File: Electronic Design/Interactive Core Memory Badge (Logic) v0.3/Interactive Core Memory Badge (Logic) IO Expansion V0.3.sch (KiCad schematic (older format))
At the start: 22 parts, among them J5 Conn_01x04_Female, J7 Conn_01x04_Male, U5 MCP23017_SO, U6 MCP23017_SO, U8 74HC14, U9 74HC14, X1 SAO_v169bis, X2 SAO_v169bis, X3 SAO_v169bis

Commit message: Add I2C Hall sensor, data sheets, sample code
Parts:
- U8, U9: value 74HC14 -> 74AC04
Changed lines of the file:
@@
 AR Path="/5EA63449/5EAA2FDC" Ref="U8"  Part="1"
 F 0 "U8" H 6000 1420 50  0000 C CNN
-F 1 "74HC14" H 6000 1327 50  0000 C CNN
+F 1 "74AC04" H 6000 1327 50  0000 C CNN
 F 2 "Digikey:SOIC-14_W3.9mm" H 6000 1100 50  0001 C CNN
-F 3 "http://www.ti.com/lit/gpn/sn74HC14" H 6000 1100 50  0001 C CNN
+F 3 "http://www.ti.com/lit/gpn/sn74AC04" H 6000 1100 50  0001 C CNN
 	1    6000 1100
 	1    0    0    -1
@@
 AR Path="/5EA63449/5EAA2FE4" Ref="U8"  Part="2"
 F 0 "U8" H 6000 1920 50  0000 C CNN
-F 1 "74HC14" H 6000 1827 50  0000 C CNN
+F 1 "74AC04" H 6000 1827 50  0000 C CNN
 F 2 "Digikey:SOIC-14_W3.9mm" H 6000 1600 50  0001 C CNN
 F 3 "http://www.ti.com/lit/gpn/sn74HC14" H 6000 1600 50  0001 C CNN
@@
 AR Path="/5EA63449/5EAA2FEA" Ref="U8"  Part="3"
 F 0 "U8" H 6000 2420 50  0000 C CNN
-F 1 "74HC14" H 6000 2327 50  0000 C CNN
+F 1 "74AC04" H 6000 2327 50  0000 C CNN
 F 2 "Digikey:SOIC-14_W3.9mm" H 6000 2100 50  0001 C CNN
-F 3 "http://www.ti.com/lit/gpn/sn74HC14" H 6000 2100 50  0001 C CNN
+F 3 "http://www.ti.com/lit/gpn/sn74AC04" H 6000 2100 50  0001 C CNN
 	3    6000 2100
 	1    0    0    -1
@@
 AR Path="/5EA63449/5EAA2FF0" Ref="U8"  Part="4"
 F 0 "U8" H 6000 2970 50  0000 C CNN
-F 1 "74HC14" H 6000 2877 50  0000 C CNN
+F 1 "74AC04" H 6000 2877 50  0000 C CNN
 F 2 "Digikey:SOIC-14_W3.9mm" H 6000 2650 50  0001 C CNN
-F 3 "http://www.ti.com/lit/gpn/sn74HC14" H 6000 2650 50  0001 C CNN
+F 3 "http://www.ti.com/lit/gpn/sn74AC04" H 6000 2650 50  0001 C CNN
 	4    6000 2650
 	1    0    0    -1
@@
 AR Path="/5EA63449/5EAA2FF6" Ref="U8"  Part="5"
 F 0 "U8" H 6000 3470 50  0000 C CNN
-F 1 "74HC14" H 6000 3377 50  0000 C CNN
+F 1 "74AC04" H 6000 3377 50  0000 C CNN
 F 2 "Digikey:SOIC-14_W3.9mm" H 6000 3150 50  0001 C CNN
-F 3 "http://www.ti.com/lit/gpn/sn74HC14" H 6000 3150 50  0001 C CNN
+F 3 "http://www.ti.com/lit/gpn/sn74AC04" H 6000 3150 50  0001 C CNN
 	5    6000 3150
 	1    0    0    -1
@@
 AR Path="/5EA63449/5EAA2FFC" Ref="U8"  Part="6"
 F 0 "U8" H 6000 4020 50  0000 C CNN
-F 1 "74HC14" H 6000 3927 50  0000 C CNN
+F 1 "74AC04" H 6000 3927 50  0000 C CNN
 F 2 "Digikey:SOIC-14_W3.9mm" H 6000 3700 50  0001 C CNN
-F 3 "http://www.ti.com/lit/gpn/sn74HC14" H 6000 3700 50  0001 C CNN
+F 3 "http://www.ti.com/lit/gpn/sn74AC04" H 6000 3700 50  0001 C CNN
 	6    6000 3700
 	1    0    0    -1
@@
 AR Path="/5EA63449/5EAA3002" Ref="U8"  Part="7"
 F 0 "U8" H 8630 1547 50  0000 L CNN
-F 1 "74HC14" H 8630 1454 50  0000 L CNN
+F 1 "74AC04" H 8630 1454 50  0000 L CNN
 F 2 "Digikey:SOIC-14_W3.9mm" H 8400 1500 50  0001 C CNN
-F 3 "http://www.ti.com/lit/gpn/sn74HC14" H 8400 1500 50  0001 C CNN
+F 3 "http://www.ti.com/lit/gpn/sn74AC04" H 8400 1500 50  0001 C CNN
 	7    8400 1500
 	1    0    0    -1
@@
 AR Path="/5EA63449/5EAA3008" Ref="U9"  Part="1"
 F 0 "U9" H 7350 1420 50  0000 C CNN
-F 1 "74HC14" H 7350 1327 50  0000 C CNN
+F 1 "74AC04" H 7350 1327 50  0000 C CNN
 F 2 "Digikey:SOIC-14_W3.9mm" H 7350 1100 50  0001 C CNN
-F 3 "http://www.ti.com/lit/gpn/sn74HC14" H 7350 1100 50  0001 C CNN
+F 3 "http://www.ti.com/lit/gpn/sn74AC04" H 7350 1100 50  0001 C CNN
 	1    7350 1100
 	1    0    0    -1
@@
 AR Path="/5EA63449/5EAA300E" Ref="U9"  Part="2"
 F 0 "U9" H 7350 1920 50  0000 C CNN
-F 1 "74HC14" H 7350 1827 50  0000 C CNN
+F 1 "74AC04" H 7350 1827 50  0000 C CNN
 F 2 "Digikey:SOIC-14_W3.9mm" H 7350 1600 50  0001 C CNN
-F 3 "http://www.ti.com/lit/gpn/sn74HC14" H 7350 1600 50  0001 C CNN
+F 3 "http://www.ti.com/lit/gpn/sn74AC04" H 7350 1600 50  0001 C CNN
 	2    7350 1600
 	1    0    0    -1
@@
 AR Path="/5EA63449/5EAA3014" Ref="U9"  Part="3"
 F 0 "U9" H 7350 2420 50  0000 C CNN
-F 1 "74HC14" H 7350 2327 50  0000 C CNN
+F 1 "74AC04" H 7350 2327 50  0000 C CNN
 F 2 "Digikey:SOIC-14_W3.9mm" H 7350 2100 50  0001 C CNN
-F 3 "http://www.ti.com/lit/gpn/sn74HC14" H 7350 2100 50  0001 C CNN
+F 3 "http://www.ti.com/lit/gpn/sn74AC04" H 7350 2100 50  0001 C CNN
 	3    7350 2100
 	1    0    0    -1
@@
 AR Path="/5EA63449/5EAA301A" Ref="U9"  Part="4"
 F 0 "U9" H 7350 2970 50  0000 C CNN
-F 1 "74HC14" H 7350 2877 50  0000 C CNN
+F 1 "74AC04" H 7350 2877 50  0000 C CNN
 F 2 "Digikey:SOIC-14_W3.9mm" H 7350 2650 50  0001 C CNN
-F 3 "http://www.ti.com/lit/gpn/sn74HC14" H 7350 2650 50  0001 C CNN
+F 3 "http://www.ti.com/lit/gpn/sn74AC04" H 7350 2650 50  0001 C CNN
 	4    7350 2650
 	1    0    0    -1
@@
 AR Path="/5EA63449/5EAA3020" Ref="U9"  Part="5"
 F 0 "U9" H 7350 3520 50  0000 C CNN
-F 1 "74HC14" H 7350 3427 50  0000 C CNN
+F 1 "74AC04" H 7350 3427 50  0000 C CNN
 F 2 "Digikey:SOIC-14_W3.9mm" H 7350 3200 50  0001 C CNN
-F 3 "http://www.ti.com/lit/gpn/sn74HC14" H 7350 3200 50  0001 C CNN
+F 3 "http://www.ti.com/lit/gpn/sn74AC04" H 7350 3200 50  0001 C CNN
 	5    7350 3200
 	1    0    0    -1
@@
 AR Path="/5EA63449/5EAA3026" Ref="U9"  Part="6"
 F 0 "U9" H 7350 4020 50  0000 C CNN
-F 1 "74HC14" H 7350 3927 50  0000 C CNN
+F 1 "74AC04" H 7350 3927 50  0000 C CNN
 F 2 "Digikey:SOIC-14_W3.9mm" H 7350 3700 50  0001 C CNN
-F 3 "http://www.ti.com/lit/gpn/sn74HC14" H 7350 3700 50  0001 C CNN
+F 3 "http://www.ti.com/lit/gpn/sn74AC04" H 7350 3700 50  0001 C CNN
 	6    7350 3700
 	1    0    0    -1
@@
 AR Path="/5EA63449/5EAA302C" Ref="U9"  Part="7"
 F 0 "U9" H 8630 3197 50  0000 L CNN
-F 1 "74HC14" H 8630 3104 50  0000 L CNN
+F 1 "74AC04" H 8630 3104 50  0000 L CNN
 F 2 "Digikey:SOIC-14_W3.9mm" H 8400 3150 50  0001 C CNN
-F 3 "http://www.ti.com/lit/gpn/sn74HC14" H 8400 3150 50  0001 C CNN
+F 3 "http://www.ti.com/lit/gpn/sn74AC04" H 8400 3150 50  0001 C CNN
 	7    8400 3150
 	1    0    0    -1

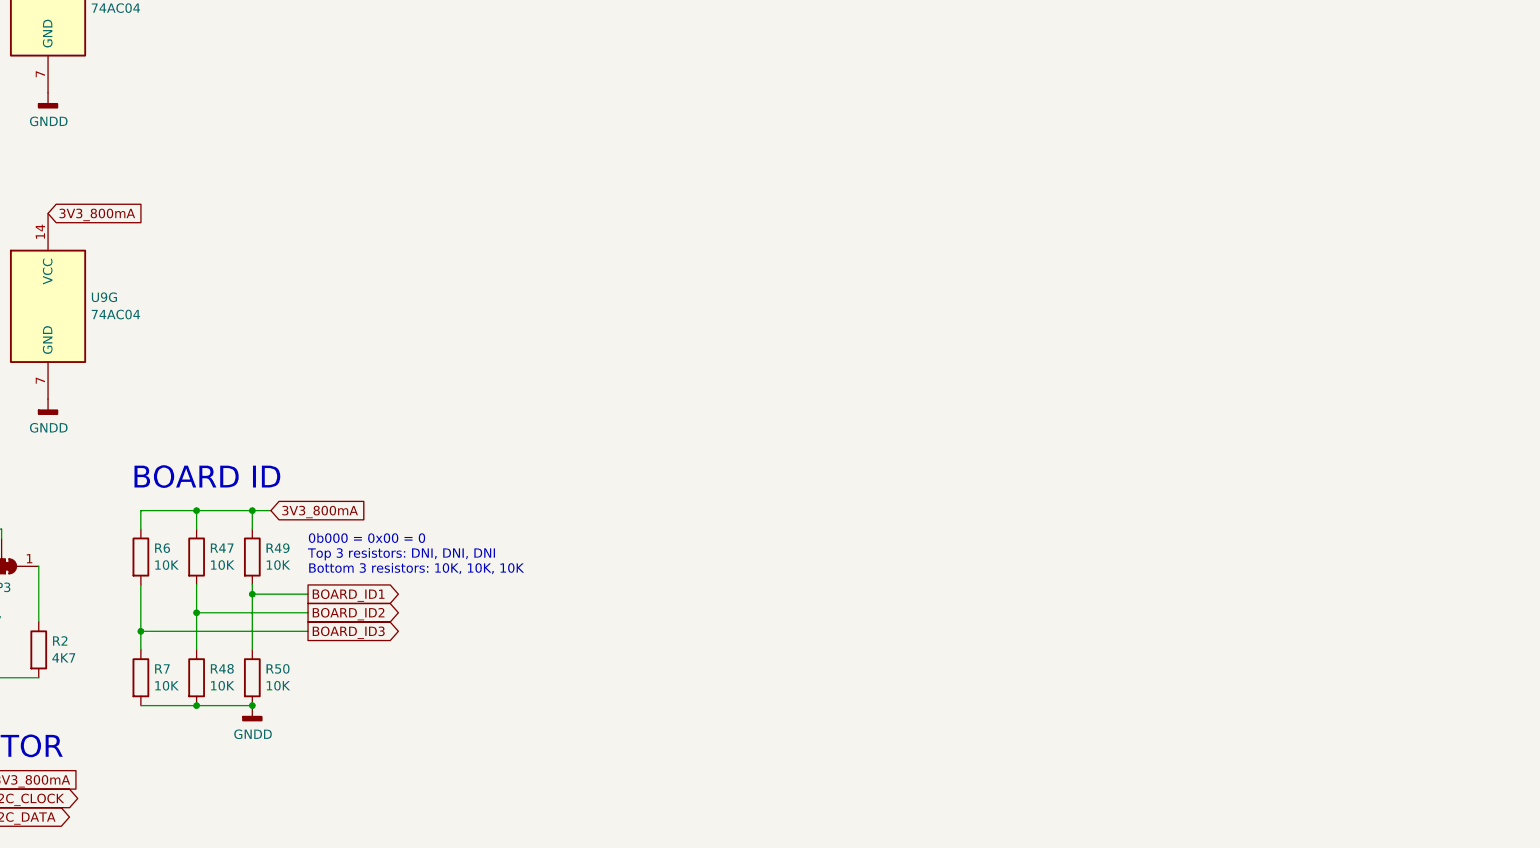
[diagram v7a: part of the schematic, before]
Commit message: Update SMD-TO pad sizes, add EEPROM, add RasPI header to LED array
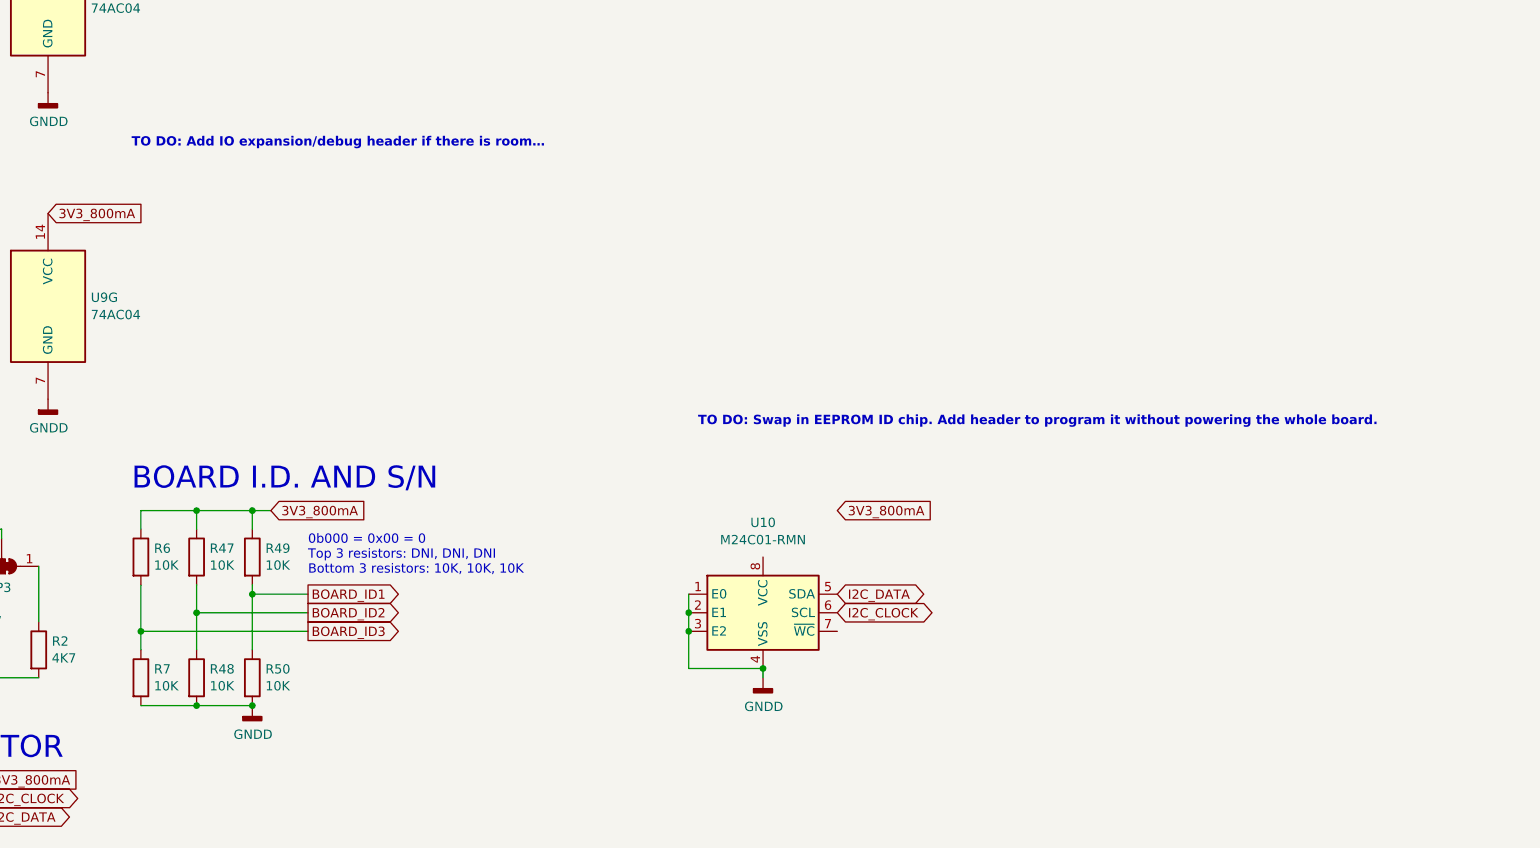
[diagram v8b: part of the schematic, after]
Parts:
- added U10: M24C01-RMN, Package_SO:SOIC-8_3.9x4.9mm_P1.27mm, symbol Memory_EEPROM:M24C01-RMN
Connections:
- net GNDD: now also U10.1 (E0), U10.2 (E1), U10.3 (E2), U10.4 (VSS)
- net I2C_CLOCK: now also U10.6 (SCL)
- net I2C_DATA: now also U10.5 (SDA)
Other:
- note added: "BOARD I.D. AND S/N"
- note added: "TO DO: Add IO expansion/debug header if there is room…"
- note added: "TO DO: Swap in EEPROM ID chip. Add header to program it without powering the whole board."
- note removed: "BOARD ID"
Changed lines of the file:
@@
 $EndComp
 Text Notes 8850 4150 0    118  ~ 0
-BOARD ID
+BOARD I.D. AND S/N
 Text GLabel 9600 4250 2    50   Input ~ 0
 3V3_800mA
@@
 Wire Wire Line
 	7850 6100 8050 6100
+Text Notes 8850 2300 0    50   ~ 10
+TO DO: Add IO expansion/debug header if there is room…
+$Comp
+L Memory_EEPROM:M24C01-RMN U?
+U 1 1 5E9366CC
+P 12250 4800
+AR Path="/5E9366CC" Ref="U?"  Part="1"
+AR Path="/5EA63449/5E9366CC" Ref="U10"  Part="1"
+F 0 "U10" H 12250 5285 50  0000 C CNN
+F 1 "M24C01-RMN" H 12250 5192 50  0000 C CNN
+F 2 "Package_SO:SOIC-8_3.9x4.9mm_P1.27mm" H 12250 5150 50  0001 C CNN
+F 3 "http://www.st.com/content/ccc/resource/technical/document/datasheet/b0/d8/50/40/5a/85/49/6f/DM00071904.pdf/files/DM00071904.pdf/jcr:content/translations/en.DM00071904.pdf" H 12300 4300 50  0001 C CNN
+	1    12250 4800
+	1    0    0    -1
+$EndComp
+Text GLabel 12650 4700 2    50   BiDi ~ 0
+I2C_DATA
+Text GLabel 12650 4800 2    50   BiDi ~ 0
+I2C_CLOCK
+Text GLabel 12650 4250 2    50   Input ~ 0
+3V3_800mA
+$Comp
+L power:GNDD #PWR0166
+U 1 1 5E93FD30
+P 12250 5150
+F 0 "#PWR0166" H 12250 4900 50  0001 C CNN
+F 1 "GNDD" H 12254 4994 50  0000 C CNN
+F 2 "" H 12250 5150 50  0001 C CNN
+F 3 "" H 12250 5150 50  0001 C CNN
+	1    12250 5150
+	1    0    0    -1
+$EndComp
+Wire Wire Line
+	11850 4700 11850 4800
+Connection ~ 11850 4800
+Wire Wire Line
+	11850 4800 11850 4900
+Wire Wire Line
+	11850 4900 11850 5100
+Wire Wire Line
+	11850 5100 12250 5100
+Connection ~ 11850 4900
+Wire Wire Line
+	12250 5100 12250 5150
+Connection ~ 12250 5100
+Text Notes 11900 3800 0    50   ~ 10
+TO DO: Swap in EEPROM ID chip. Add header to program it without powering the whole board.
 $EndSCHEMATC
